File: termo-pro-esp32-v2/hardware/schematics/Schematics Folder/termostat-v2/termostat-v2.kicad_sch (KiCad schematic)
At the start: 22 parts, among them J1 Conn_01x08_Pin, Q1 PN2222A, Q2 PN2222A, SW1 SW_Push, SW2 SW_Push, SW3 SW_Push, SW4 SW_Push, U1 NODEMCU-32S, U2 DHT11

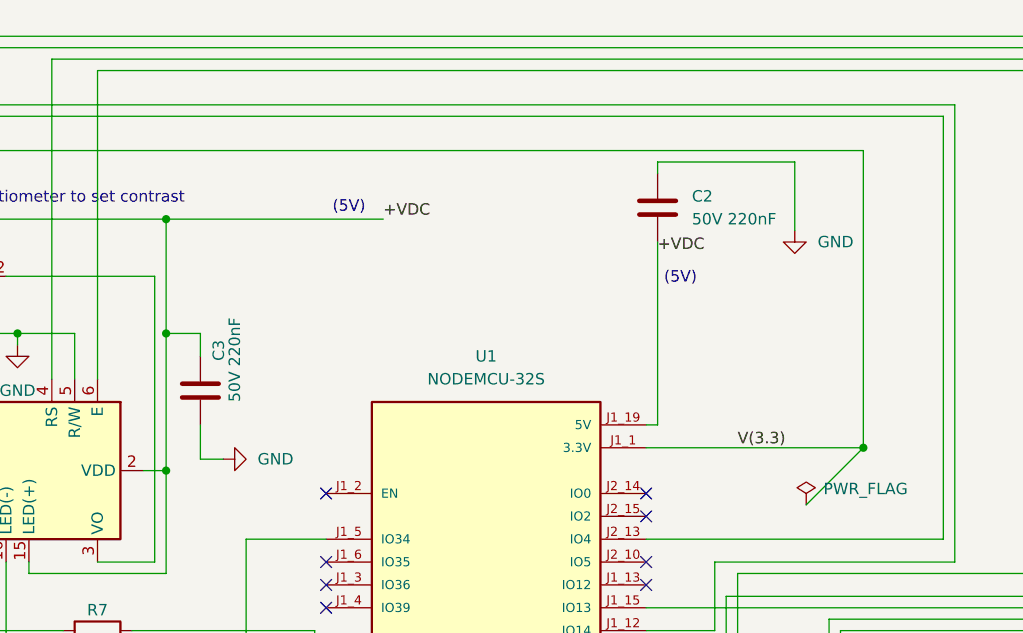
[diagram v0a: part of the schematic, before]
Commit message: Hardware part of the project is finished.
-DHT11 placement on thermostat unit fixed, pins trace redone.
-USB-C port on thermostat unit placed closer to edge by 4mm.
-Capacitors values recalculated and updated to closest common values, resistors values too.
-Starting unit pcb redone traces as relay and caps have been moved to the back plate.

-Starting & thermostat units PCB are done, inspected.
-Ready for fabrication.
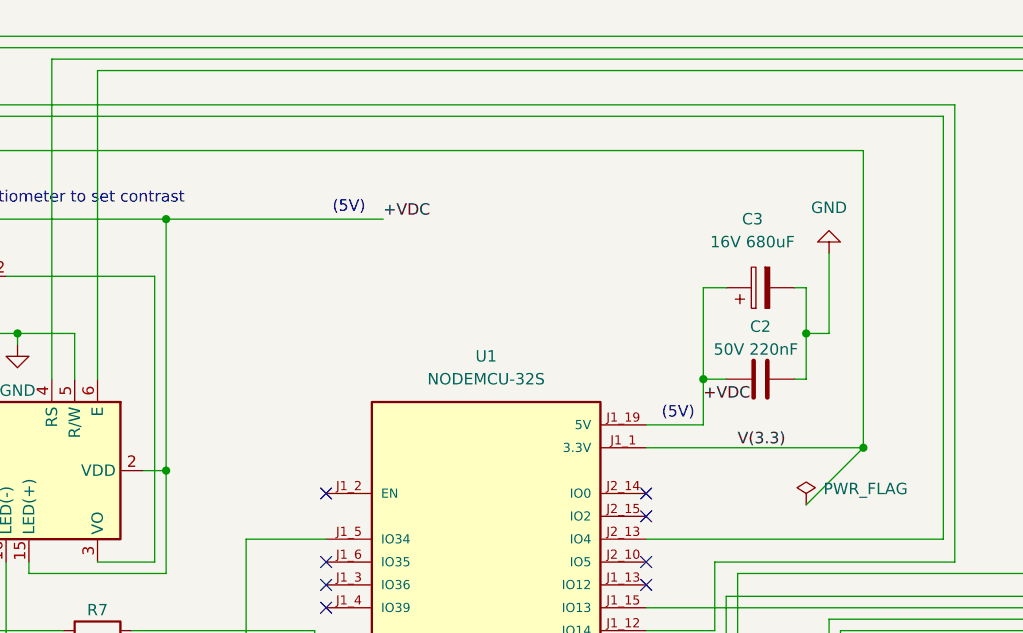
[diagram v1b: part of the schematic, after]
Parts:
- removed C3: 50V 220nF, Capacitor_THT:C_Disc_D11.0mm_W5.0mm_P5.00mm, symbol Device:C
- added C3: 16V 680uF, Capacitor_THT:CP_Radial_D8.0mm_P5.00mm, symbol Device:C_Polarized
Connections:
- net +VDC: now also C2.1, C3.1; no longer C2.2
- net GND: now also C2.2, C3.2; no longer C2.1
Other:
- moved on the sheet: C2
